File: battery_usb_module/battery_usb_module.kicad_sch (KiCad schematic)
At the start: 3 parts, among them J1 USB_C_Receptacle_USB2.0_16P, J2 DF12NC_3.0_-60DS-0.5V_51_, U1 LP3947

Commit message: Battery Charger Wiring (WIP)
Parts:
- added C1: 10uF, symbol Device:C_US
- added C2: 1uF, symbol Device:C_US
- added J3: Conn_01x02_MountingPin, symbol Connector_Generic_MountingPin:Conn_01x02_MountingPin
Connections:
- net at U1.14 (CHG_IN): now also J1.A4 (VBUS), J1.A9 (VBUS), J1.B4 (VBUS), J1.B9 (VBUS), J2.4, C2.2
- net at U1.4 (BATT): now also U1.6 (VB_{SENSE}), C1.2, J3.1 (Pin_1)
- new net GND: C1.1, C2.1, J3.2 (Pin_2)

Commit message: PCB layout for battery/usb module
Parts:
- C1, C2: footprint (none) -> Capacitor_SMD:C_0603_1608Metric
- J1: footprint (none) -> Connector_USB:USB_C_Receptacle_GCT_USB4105-xx-A_16P_TopMnt_Horizontal
- J2: footprint DF12NC_3.0_-60DS-0.5V_51_:HRS_DF12NC_3.0_-60DS-0.5V_51_ -> Connector_Hirose:Hirose_DF12_DF12E3.0-60DP-0.5V_2x30_P0.50mm_Vertical
- J3: footprint (none) -> Connector_PinHeader_1.00mm:PinHeader_1x02_P1.00mm_Vertical_SMD_Pin1Left
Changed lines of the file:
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@@
 			)
 		)
-		(property "Footprint" ""
+		(property "Footprint" "Capacitor_SMD:C_0603_1608Metric"
 			(at 152.4 68.58 0)
 			(effects
@@
 			)
 		)
-		(property "Footprint" ""
+		(property "Footprint" "Connector_PinHeader_1.00mm:PinHeader_1x02_P1.00mm_Vertical_SMD_Pin1Left"
 			(at 180.34 116.84 0)
 			(effects
@@
 			)
 		)
-		(property "Footprint" "DF12NC_3.0_-60DS-0.5V_51_:HRS_DF12NC_3.0_-60DS-0.5V_51_"
+		(property "Footprint" "Connector_Hirose:Hirose_DF12_DF12E3.0-60DP-0.5V_2x30_P0.50mm_Vertical"
 			(at 242.57 96.52 0)
 			(effects
@@
 			)
 		)
-		(property "Footprint" ""
+		(property "Footprint" "Connector_USB:USB_C_Receptacle_GCT_USB4105-xx-A_16P_TopMnt_Horizontal"
 			(at 110.49 88.9 0)
 			(effects
@@
 			)
 		)
-		(property "Footprint" ""
+		(property "Footprint" "Capacitor_SMD:C_0603_1608Metric"
 			(at 177.8 68.58 0)
 			(effects

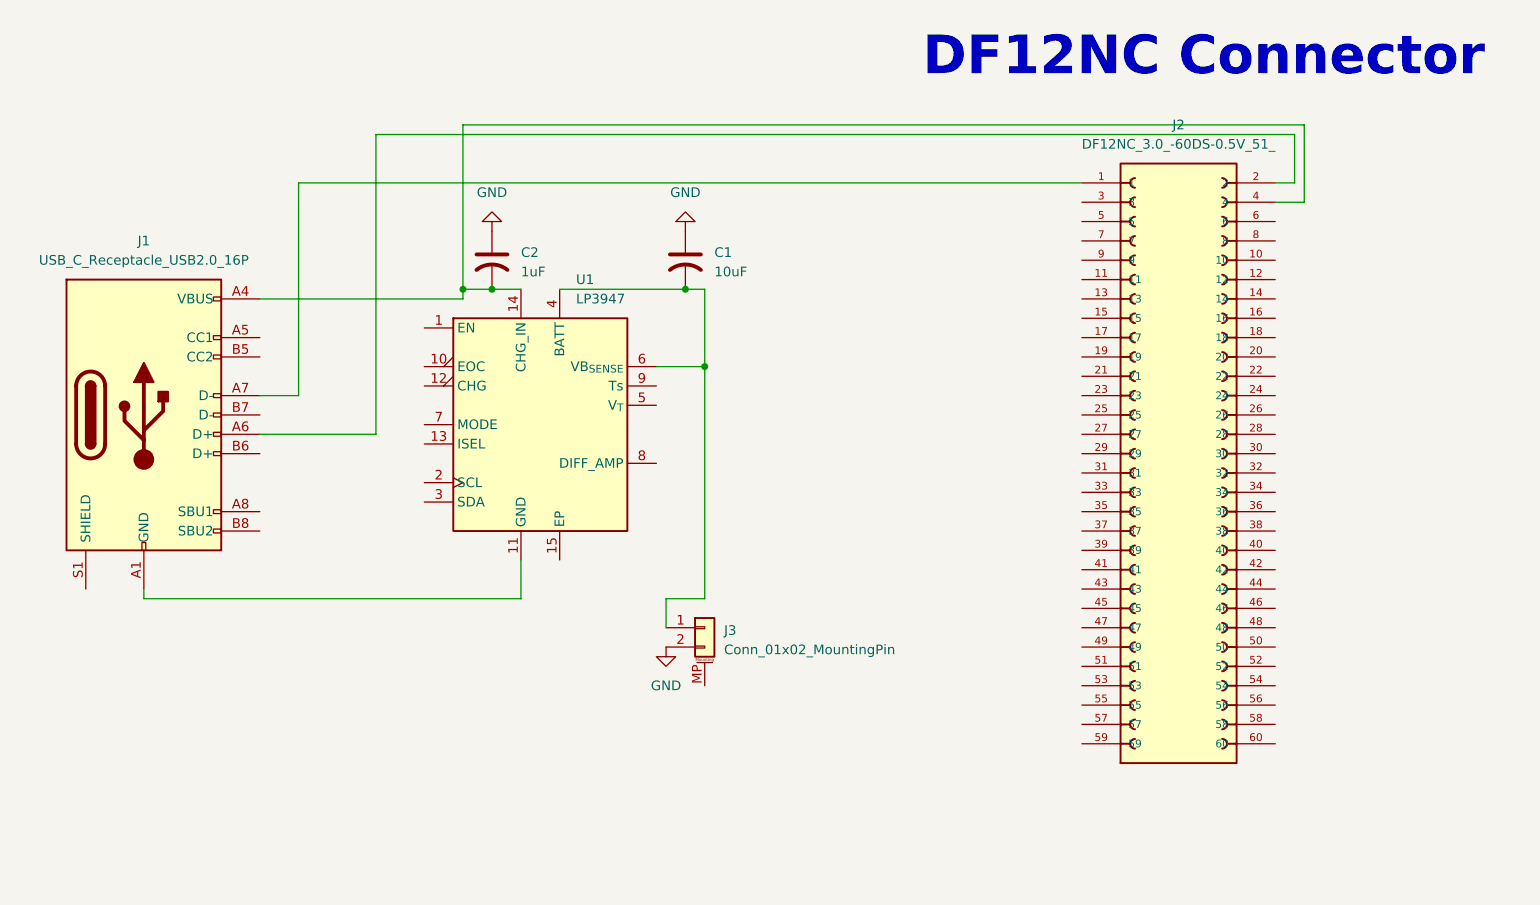
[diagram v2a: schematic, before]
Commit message: Move connector in battery module ,new usb-c footprint and symbol in pcb and schematic, fixed wrong capacitor values, and redid some wiring on battery module
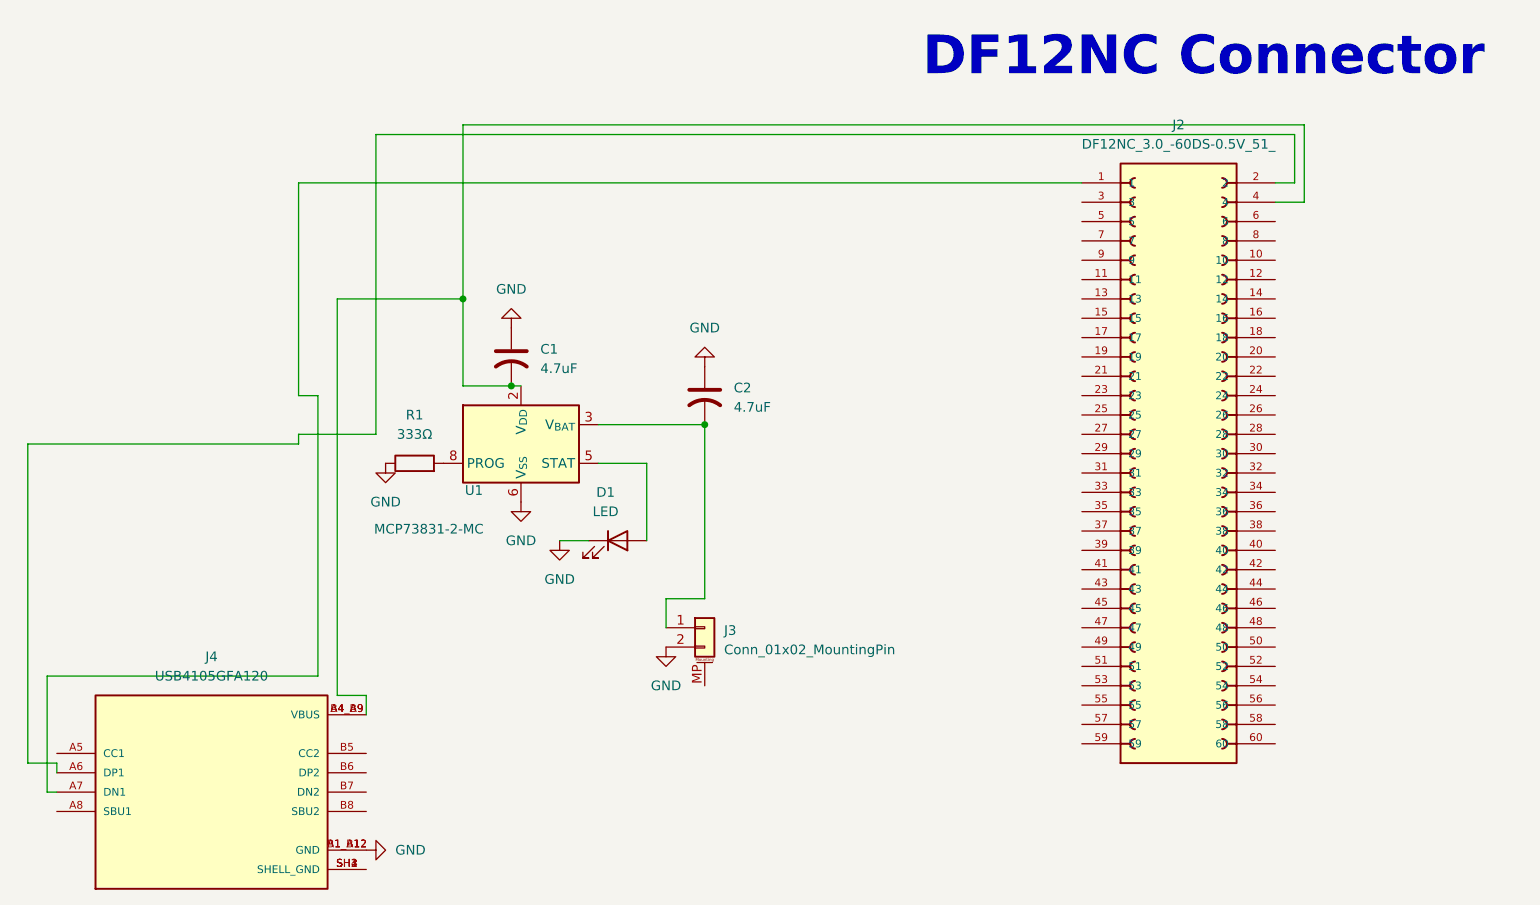
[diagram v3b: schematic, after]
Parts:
- removed J1: USB_C_Receptacle_USB2.0_16P, Connector_USB:USB_C_Receptacle_GCT_USB4105-xx-A_16P_TopMnt_Horizontal, symbol Connector:USB_C_Receptacle_USB2.0_16P
- removed U1: LP3947, Package_SON:WSON-14-1EP_4.0x4.0mm_P0.5mm_EP2.6x2.6mm, symbol Battery_Management:LP3947
- added D1: LED, LED_SMD:LED_0603_1608Metric, symbol Device:LED
- added J4: USB4105GFA120, USB4105GFA120:GCT_USB4105GFA120, symbol USB4105GFA120:USB4105GFA120
- added R1: 333Ω, Resistor_SMD:R_0603_1608Metric, symbol Device:R
- added U1: MCP73831-2-MC, Package_DFN_QFN:DFN-8-1EP_3x2mm_P0.5mm_EP1.7x1.4mm, symbol Battery_Management:MCP73831-2-MC
- C1: value 10uF -> 4.7uF
- C2: value 1uF -> 4.7uF
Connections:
- net GND: now also D1.1 (K), J4.A1_B12 (GND), J4.B1_A12 (GND), R1.1, U1.6 (V_{SS})
- net at J2.4: now also C1.2, J4.A4_B9 (VBUS), J4.B4_A9 (VBUS), U1.1 (V_{DD}), U1.2 (V_{DD}); no longer C2.2
- net at J3.1 (Pin_1): now also C2.2, U1.3 (V_{BAT}), U1.4 (V_{BAT}); no longer C1.2
- net at J2.1: now also J4.A7 (DN1)
- net at J2.2: now also J4.A6 (DP1)
- new net: D1.2 (A), U1.5 (STAT)
- new net: R1.2, U1.8 (PROG)
- new net: J4.SH1 (SHELL_GND), J4.SH2 (SHELL_GND), J4.SH3 (SHELL_GND), J4.SH4 (SHELL_GND)
